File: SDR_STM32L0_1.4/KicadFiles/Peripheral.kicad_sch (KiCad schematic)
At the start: 25 parts, among them J1 Conn_01x03, J2 USB_C_Receptacle_USB2.0_16P, J3 Conn_01x03, J4 Conn_01x03, J5 Conn_01x03, P1 3220-20-0200-00, SW2 RESET SWITCH, U2 Engine-Controller_SST25VF040B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, U5 CP2102N-Axx-xQFN28

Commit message: begin routing
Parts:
- SW2: footprint Button_Switch_THT:SW_DIP_SPSTx01_Slide_9.78x4.72mm_W7.62mm_P2.54mm -> Button_Switch_THT:SW_DIP_SPSTx01_Slide_6.7x4.1mm_W7.62mm_P2.54mm_LowProfile
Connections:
- net GPIO1_ADC: now also J1.1 (Pin_1); no longer J1.3 (Pin_3)
- net GPIO1_INPUT: now also J1.3 (Pin_3); no longer J1.1 (Pin_1)
- net GPIO2_ADC: now also J3.1 (Pin_1); no longer J3.3 (Pin_3)
- net GPIO2_INPUT: now also J3.3 (Pin_3); no longer J3.1 (Pin_1)
- net GPIO3_ADC: now also J4.1 (Pin_1); no longer J4.3 (Pin_3)
- net GPIO3_INPUT: now also J4.3 (Pin_3); no longer J4.1 (Pin_1)
- net GPIO4_ADC: now also J5.1 (Pin_1); no longer J5.3 (Pin_3)
- net GPIO4_INPUT: now also J5.3 (Pin_3); no longer J5.1 (Pin_1)
- net SPI1_NSS renamed SPI1_NSS***********

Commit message: Finished PCB Routing
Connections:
- net SPI1_NSS*********** renamed SPI1_NSS
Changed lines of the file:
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@@
 		)
 	)
-	(global_label "SPI1_NSS***********"
+	(global_label "SPI1_NSS"
 		(shape input)
 		(at 153.035 31.75 180)
@@
 		)
 		(property "Intersheetrefs" "${INTERSHEET_REFS}"
-			(at 130.3953 31.75 0)
+			(at 141.0389 31.75 0)
 			(effects
 				(font

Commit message: 1.5
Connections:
- net USART2_CTS renamed ROUTPUT
- net USART2_RX renamed GOUTPUT
- net USART2_TX renamed BOUTPUT
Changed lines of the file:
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@@
 		)
 	)
-	(global_label "USART2_CTS"
+	(global_label "ROUTPUT"
 		(shape input)
 		(at 74.93 149.86 180)
@@
 		)
 		(property "Intersheetrefs" "${INTERSHEET_REFS}"
-			(at 60.4544 149.86 0)
+			(at 63.4781 149.86 0)
 			(effects
 				(font
@@
 		)
 	)
-	(global_label "USART2_TX"
+	(global_label "BOUTPUT"
 		(shape input)
 		(at 87.63 154.94 180)
@@
 		)
 		(property "Intersheetrefs" "${INTERSHEET_REFS}"
-			(at 74.4244 154.94 0)
+			(at 76.1781 154.94 0)
 			(effects
 				(font
@@
 		)
 	)
-	(global_label "USART2_RX"
+	(global_label "GOUTPUT"
 		(shape input)
 		(at 81.28 152.4 180)
@@
 		)
 		(property "Intersheetrefs" "${INTERSHEET_REFS}"
-			(at 67.772 152.4 0)
-			(effects
-				(font
+			(at 69.8281 152.4 0)
+			(effects
+				(font

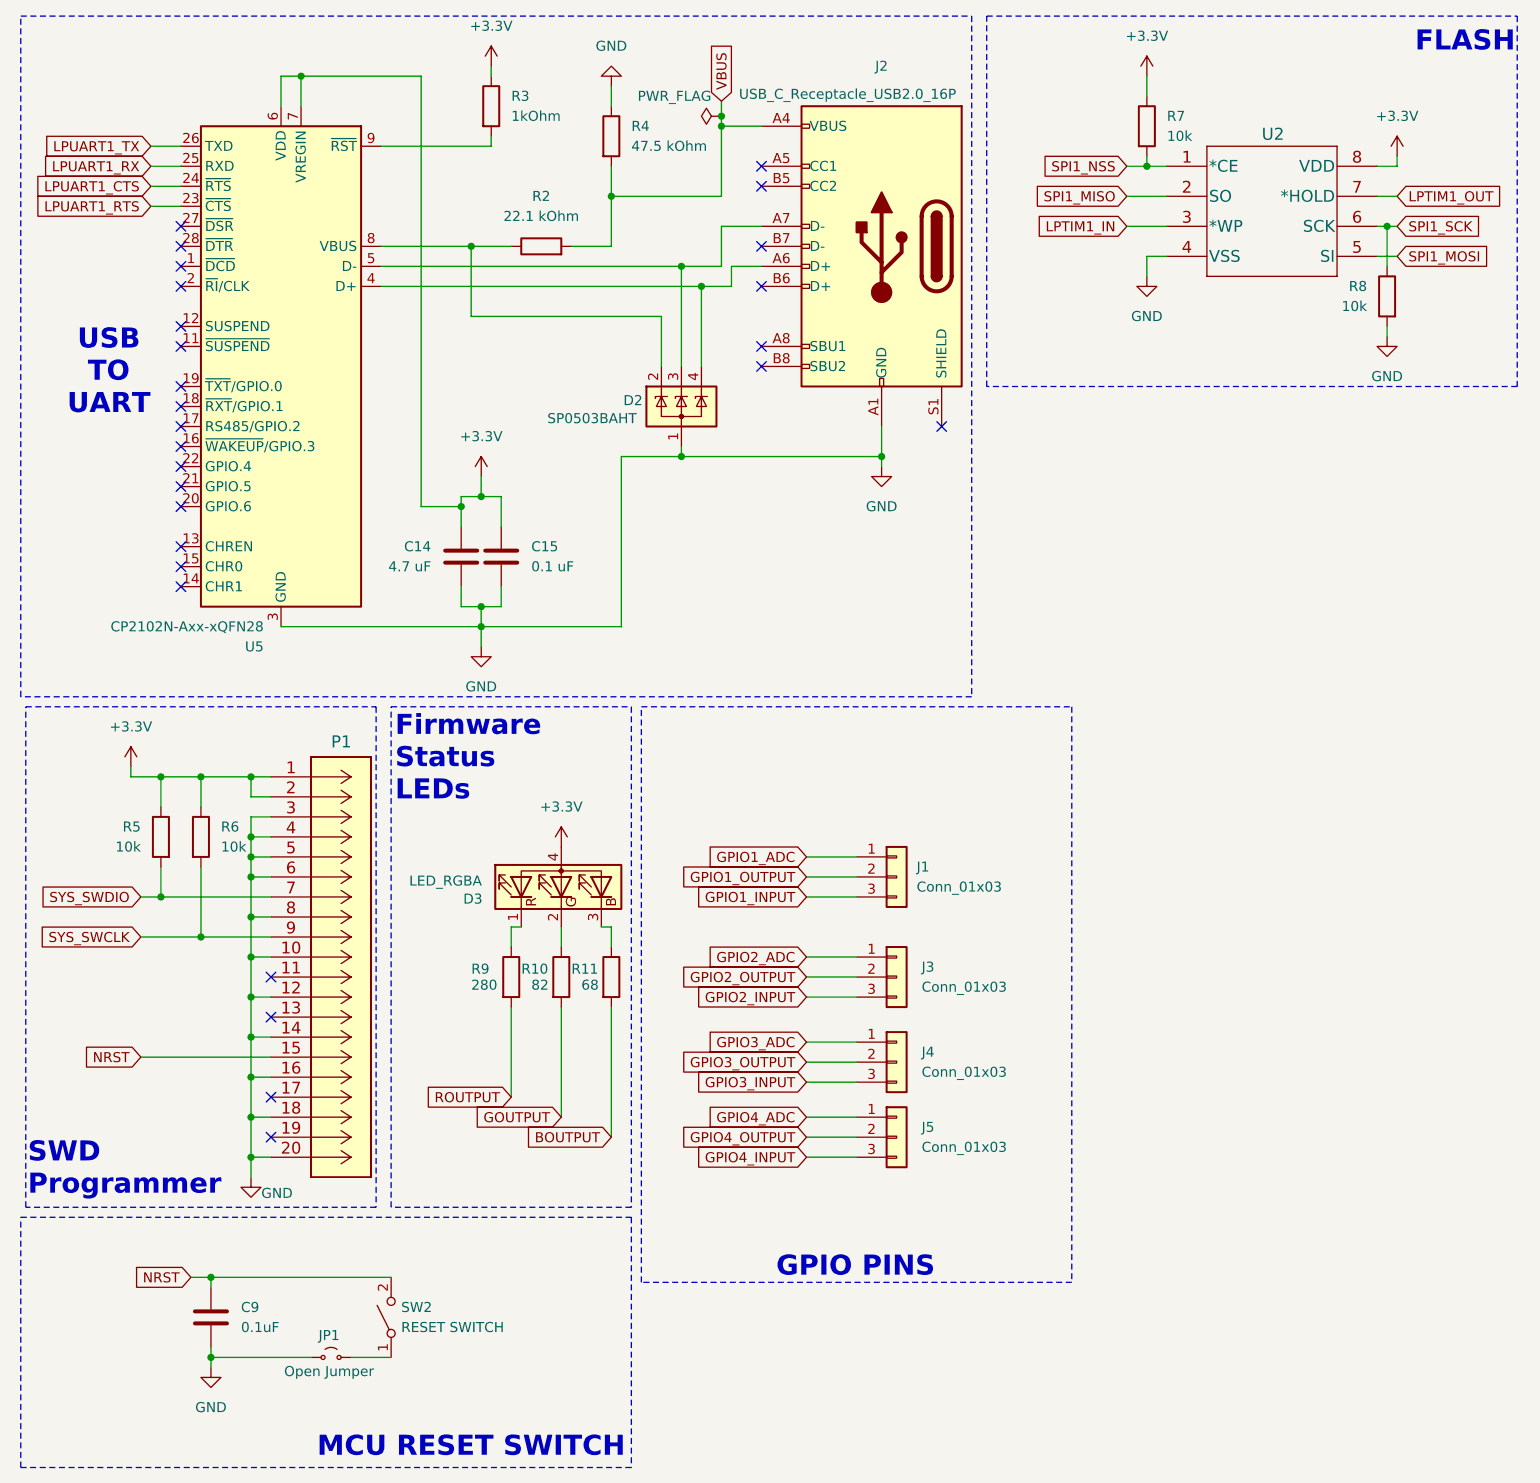
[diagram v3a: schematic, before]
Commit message: Upgrade
Changed a few peripherals (less ports, +/- on ports, switched jumpers, switched pinouts), and made new shematic
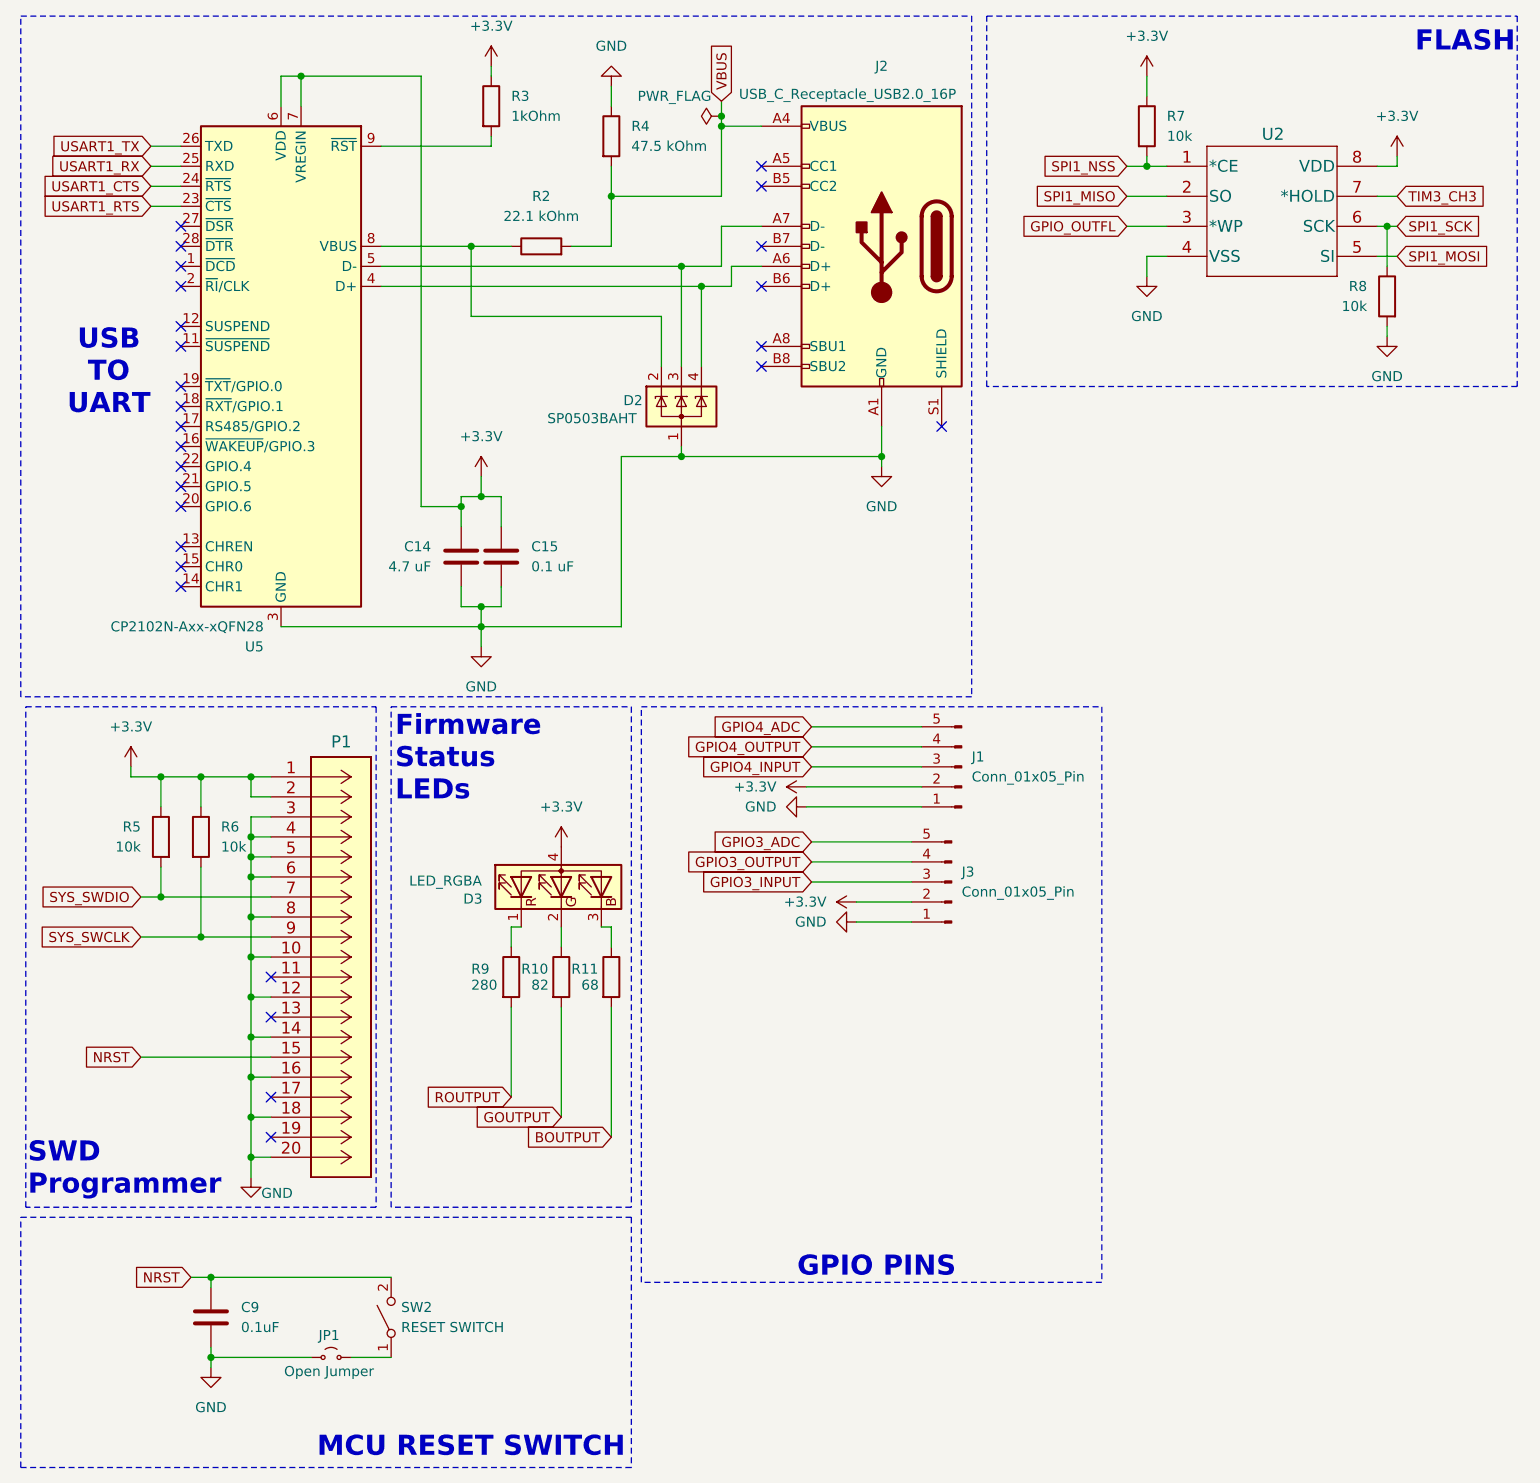
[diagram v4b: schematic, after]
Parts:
- removed J1: Conn_01x03, Connector_JST:JST_EH_S3B-EH_1x03_P2.50mm_Horizontal, symbol Connector_Generic:Conn_01x03
- removed J3, J4, J5: Conn_01x03, Connector_PinSocket_1.00mm:PinSocket_1x03_P1.00mm_Vertical, symbol Connector_Generic:Conn_01x03
- added J1, J3: Conn_01x05_Pin, 19351990:CONN_1935190_PXC, symbol Connector:Conn_01x05_Pin
- C15, C9: footprint Capacitor_SMD:C_0402_1005Metric -> Capacitor_SMD:C_0603_1608Metric
- D3: footprint FlightComputer:CLMVC-FKA-CL1D1L71BB7C3C3 -> FCMac:CLMVC-FKA-CL1D1L71BB7C3C3
- JP1: footprint TestPoint:TestPoint_2Pads_Pitch2.54mm_Drill0.8mm -> Resistor_SMD:R_0603_1608Metric
- P1: footprint FlightComputer:3220-20-0200-00 -> FCMac:3220-20-0200-00
- R10, R11, R3, R5, R6, R7, R8, R9: footprint Resistor_SMD:R_0402_1005Metric -> Resistor_SMD:R_0603_1608Metric
- SW2: footprint Button_Switch_THT:SW_DIP_SPSTx01_Slide_6.7x4.1mm_W7.62mm_P2.54mm_LowProfile -> Button_Switch_SMD:SW_SPST_PTS647_Sx38
- U2: footprint FlightComputer:SST25VF040B-50-4I-S2AE-T -> FCMac:SST25VF040B-50-4I-S2AE-T
- U5: footprint Package_DFN_QFN:QFN-28-1EP_5x5mm_P0.5mm_EP3.35x3.35mm -> CP2102N:QFN28_5X5_SIL
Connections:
- net +3.3V: now also J1.2 (Pin_2), J3.2 (Pin_2)
- net GND: now also J1.1 (Pin_1), J3.1 (Pin_1)
- net GPIO3_ADC: now also J3.5 (Pin_5)
- net GPIO3_INPUT: now also J3.3 (Pin_3)
- net GPIO3_OUTPUT: now also J3.4 (Pin_4)
- net GPIO4_ADC: now also J1.5 (Pin_5)
- net GPIO4_INPUT: now also J1.3 (Pin_3)
- net GPIO4_OUTPUT: now also J1.4 (Pin_4)
- net LPTIM1_IN renamed GPIO_OUTFL
- net LPTIM1_OUT renamed TIM3_CH3
- net LPUART1_CTS renamed USART1_CTS
- net LPUART1_RTS renamed USART1_RTS
- net LPUART1_RX renamed USART1_RX
- net LPUART1_TX renamed USART1_TX
